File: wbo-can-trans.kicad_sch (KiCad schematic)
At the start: 7 parts, among them U15 TJA1051T-3

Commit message: Modified IGBTs and routed smart coils
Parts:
- renumbered C16 to C12, C17 to C13, C18 to C14, C19 to C15, D2 to D1, R16 to R15, U15 to U13
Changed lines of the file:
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@@
   (symbol (lib_id "Power_Protection:NUP2105L") (at 146.05 96.52 0) (mirror y)
     (in_bom yes) (on_board yes)
-    (property "Reference" "D2" (id 0) (at 140.97 95.25 0)
+    (property "Reference" "D1" (id 0) (at 140.97 95.25 0)
       (effects (font (size 1.27 1.27)) (justify left))
     )
@@
   (symbol (lib_id "Device:C") (at 105.41 77.47 0) (mirror y)
     (in_bom yes) (on_board yes)
-    (property "Reference" "C16" (id 0) (at 102.489 76.3016 0)
+    (property "Reference" "C12" (id 0) (at 102.489 76.3016 0)
       (effects (font (size 1.27 1.27)) (justify left))
     )
@@
   (symbol (lib_id "Device:C") (at 105.41 95.25 0) (mirror y)
     (in_bom yes) (on_board yes)
-    (property "Reference" "C17" (id 0) (at 102.489 94.0816 0)
+    (property "Reference" "C13" (id 0) (at 102.489 94.0816 0)
       (effects (font (size 1.27 1.27)) (justify left))
     )
@@
   (symbol (lib_id "Device:C") (at 190.5 93.98 0) (mirror y)
     (in_bom yes) (on_board yes)
-    (property "Reference" "C18" (id 0) (at 196.85 92.71 0)
+    (property "Reference" "C14" (id 0) (at 196.85 92.71 0)
       (effects (font (size 1.27 1.27)) (justify left))
     )
@@
   (symbol (lib_id "Device:C") (at 200.66 93.98 0) (mirror y)
     (in_bom yes) (on_board yes)
-    (property "Reference" "C19" (id 0) (at 207.01 92.71 0)
+    (property "Reference" "C15" (id 0) (at 207.01 92.71 0)
       (effects (font (size 1.27 1.27)) (justify left))
     )
@@
   (symbol (lib_id "Interface_CAN_LIN:TJA1051T-3") (at 166.37 86.36 0) (mirror y)
     (in_bom yes) (on_board yes)
-    (property "Reference" "U15" (id 0) (at 156.21 73.66 0))
+    (property "Reference" "U13" (id 0) (at 156.21 73.66 0))
     (property "Value" "TJA1051T-3" (id 1) (at 160.02 76.2 0))
     (property "Footprint" "Package_SO:SOIC-8_3.9x4.9mm_P1.27mm" (id 2) (at 166.37 99.06 0)
@@
   (symbol (lib_id "Device:R") (at 115.57 86.36 90) (mirror x)
     (in_bom no) (on_board yes)
-    (property "Reference" "R16" (id 0) (at 115.57 80.01 90))
+    (property "Reference" "R15" (id 0) (at 115.57 80.01 90))
     (property "Value" "120" (id 1) (at 115.57 82.55 90))
     (property "Footprint" "Resistor_SMD:R_1206_3216Metric" (id 2) (at 115.57 84.582 90)

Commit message: All fixed up for JLC
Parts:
- C16: renamed from C12; LCSC C1567 -> C14857
- C17: renamed from C13; LCSC C1567 -> C14857
- C18: renamed from C14; LCSC C1525 -> C49678
- C19: renamed from C15; LCSC C1525 -> C49678
- renumbered D1 to D2, R15 to R16, U13 to U15
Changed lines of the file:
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@@
   (symbol (lib_id "Power_Protection:NUP2105L") (at 146.05 96.52 0) (mirror y)
     (in_bom yes) (on_board yes)
-    (property "Reference" "D1" (id 0) (at 140.97 95.25 0)
+    (property "Reference" "D2" (id 0) (at 140.97 95.25 0)
       (effects (font (size 1.27 1.27)) (justify left))
     )
@@
   (symbol (lib_id "Device:C") (at 105.41 77.47 0) (mirror y)
     (in_bom yes) (on_board yes)
-    (property "Reference" "C12" (id 0) (at 102.489 76.3016 0)
+    (property "Reference" "C16" (id 0) (at 102.489 76.3016 0)
       (effects (font (size 1.27 1.27)) (justify left))
     )
@@
       (effects (font (size 1.27 1.27)) hide)
     )
-    (property "LCSC" "C1567" (id 4) (at 105.41 77.47 0)
+    (property "LCSC" "C14857" (id 4) (at 105.41 77.47 0)
       (effects (font (size 1.27 1.27)) hide)
     )
@@
   (symbol (lib_id "Device:C") (at 105.41 95.25 0) (mirror y)
     (in_bom yes) (on_board yes)
-    (property "Reference" "C13" (id 0) (at 102.489 94.0816 0)
+    (property "Reference" "C17" (id 0) (at 102.489 94.0816 0)
       (effects (font (size 1.27 1.27)) (justify left))
     )
@@
       (effects (font (size 1.27 1.27)) hide)
     )
-    (property "LCSC" "C1567" (id 4) (at 105.41 95.25 0)
+    (property "LCSC" "C14857" (id 4) (at 105.41 95.25 0)
       (effects (font (size 1.27 1.27)) hide)
     )
@@
   (symbol (lib_id "Device:C") (at 190.5 93.98 0) (mirror y)
     (in_bom yes) (on_board yes)
-    (property "Reference" "C14" (id 0) (at 196.85 92.71 0)
+    (property "Reference" "C18" (id 0) (at 196.85 92.71 0)
       (effects (font (size 1.27 1.27)) (justify left))
     )
@@
       (effects (font (size 1.27 1.27)) hide)
     )
-    (property "LCSC" "C1525" (id 4) (at 190.5 93.98 0)
+    (property "LCSC" "C49678" (id 4) (at 190.5 93.98 0)
       (effects (font (size 1.27 1.27)) hide)
     )
@@
   (symbol (lib_id "Device:C") (at 200.66 93.98 0) (mirror y)
     (in_bom yes) (on_board yes)
-    (property "Reference" "C15" (id 0) (at 207.01 92.71 0)
+    (property "Reference" "C19" (id 0) (at 207.01 92.71 0)
       (effects (font (size 1.27 1.27)) (justify left))
     )
@@
       (effects (font (size 1.27 1.27)) hide)
     )
-    (property "LCSC" "C1525" (id 4) (at 200.66 93.98 0)
+    (property "LCSC" "C49678" (id 4) (at 200.66 93.98 0)
       (effects (font (size 1.27 1.27)) hide)
     )
@@
   (symbol (lib_id "Interface_CAN_LIN:TJA1051T-3") (at 166.37 86.36 0) (mirror y)
     (in_bom yes) (on_board yes)
-    (property "Reference" "U13" (id 0) (at 156.21 73.66 0))
+    (property "Reference" "U15" (id 0) (at 156.21 73.66 0))
     (property "Value" "TJA1051T-3" (id 1) (at 160.02 76.2 0))
     (property "Footprint" "Package_SO:SOIC-8_3.9x4.9mm_P1.27mm" (id 2) (at 166.37 99.06 0)
@@
   (symbol (lib_id "Device:R") (at 115.57 86.36 90) (mirror x)
     (in_bom no) (on_board yes)
-    (property "Reference" "R15" (id 0) (at 115.57 80.01 90))
+    (property "Reference" "R16" (id 0) (at 115.57 80.01 90))
     (property "Value" "120" (id 1) (at 115.57 82.55 90))
     (property "Footprint" "Resistor_SMD:R_1206_3216Metric" (id 2) (at 115.57 84.582 90)

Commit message: Fixed 12V_RAW and added grounds for sensors
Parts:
- renumbered C16 to C12, C17 to C13, C18 to C14, C19 to C15, D2 to D1, R16 to R15, U15 to U13
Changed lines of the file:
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@@
   (symbol (lib_name "GND_22") (lib_id "power:GND") (at 105.41 99.06 0) (mirror y)
     (in_bom yes) (on_board yes)
-    (property "Reference" "#PWR0124" (id 0) (at 105.41 105.41 0)
+    (property "Reference" "#PWR0111" (id 0) (at 105.41 105.41 0)
       (effects (font (size 1.27 1.27)) hide)
     )
@@
   (symbol (lib_name "GND_24") (lib_id "power:GND") (at 166.37 96.52 0) (mirror y)
     (in_bom yes) (on_board yes)
-    (property "Reference" "#PWR0118" (id 0) (at 166.37 102.87 0)
+    (property "Reference" "#PWR0105" (id 0) (at 166.37 102.87 0)
       (effects (font (size 1.27 1.27)) hide)
     )
@@
   (symbol (lib_name "GND_27") (lib_id "power:GND") (at 181.61 91.44 90) (mirror x)
     (in_bom yes) (on_board yes)
-    (property "Reference" "#PWR0117" (id 0) (at 187.96 91.44 0)
+    (property "Reference" "#PWR0104" (id 0) (at 187.96 91.44 0)
       (effects (font (size 1.27 1.27)) hide)
     )
@@
   (symbol (lib_id "Power_Protection:NUP2105L") (at 146.05 96.52 0) (mirror y)
     (in_bom yes) (on_board yes)
-    (property "Reference" "D2" (id 0) (at 140.97 95.25 0)
+    (property "Reference" "D1" (id 0) (at 140.97 95.25 0)
       (effects (font (size 1.27 1.27)) (justify left))
     )
@@
   (symbol (lib_id "Device:C") (at 105.41 77.47 0) (mirror y)
     (in_bom yes) (on_board yes)
-    (property "Reference" "C16" (id 0) (at 102.489 76.3016 0)
+    (property "Reference" "C12" (id 0) (at 102.489 76.3016 0)
       (effects (font (size 1.27 1.27)) (justify left))
     )
@@
   (symbol (lib_name "GND_25") (lib_id "power:GND") (at 190.5 99.06 0) (mirror y)
     (in_bom yes) (on_board yes)
-    (property "Reference" "#PWR0123" (id 0) (at 190.5 105.41 0)
+    (property "Reference" "#PWR0110" (id 0) (at 190.5 105.41 0)
       (effects (font (size 1.27 1.27)) hide)
     )
@@
   (symbol (lib_name "GND_21") (lib_id "power:GND") (at 105.41 73.66 0) (mirror x)
     (in_bom yes) (on_board yes)
-    (property "Reference" "#PWR0125" (id 0) (at 105.41 67.31 0)
+    (property "Reference" "#PWR0112" (id 0) (at 105.41 67.31 0)
       (effects (font (size 1.27 1.27)) hide)
     )
@@
   (symbol (lib_name "GND_26") (lib_id "power:GND") (at 200.66 99.06 0) (mirror y)
     (in_bom yes) (on_board yes)
-    (property "Reference" "#PWR0122" (id 0) (at 200.66 105.41 0)
+    (property "Reference" "#PWR0109" (id 0) (at 200.66 105.41 0)
       (effects (font (size 1.27 1.27)) hide)
     )
@@
   (symbol (lib_id "Device:C") (at 105.41 95.25 0) (mirror y)
     (in_bom yes) (on_board yes)
-    (property "Reference" "C17" (id 0) (at 102.489 94.0816 0)
+    (property "Reference" "C13" (id 0) (at 102.489 94.0816 0)
       (effects (font (size 1.27 1.27)) (justify left))
     )
@@
   (symbol (lib_id "Device:C") (at 190.5 93.98 0) (mirror y)
     (in_bom yes) (on_board yes)
-    (property "Reference" "C18" (id 0) (at 196.85 92.71 0)
+    (property "Reference" "C14" (id 0) (at 196.85 92.71 0)
       (effects (font (size 1.27 1.27)) (justify left))
     )
@@
   (symbol (lib_id "Device:C") (at 200.66 93.98 0) (mirror y)
     (in_bom yes) (on_board yes)
-    (property "Reference" "C19" (id 0) (at 207.01 92.71 0)
+    (property "Reference" "C15" (id 0) (at 207.01 92.71 0)
       (effects (font (size 1.27 1.27)) (justify left))
     )
@@
   (symbol (lib_id "Interface_CAN_LIN:TJA1051T-3") (at 166.37 86.36 0) (mirror y)
     (in_bom yes) (on_board yes)
-    (property "Reference" "U15" (id 0) (at 156.21 73.66 0))
+    (property "Reference" "U13" (id 0) (at 156.21 73.66 0))
     (property "Value" "TJA1051T-3" (id 1) (at 160.02 76.2 0))
     (property "Footprint" "Package_SO:SOIC-8_3.9x4.9mm_P1.27mm" (id 2) (at 166.37 99.06 0)
@@
   (symbol (lib_name "GND_23") (lib_id "power:GND") (at 146.05 102.87 0) (mirror y)
     (in_bom yes) (on_board yes)
-    (property "Reference" "#PWR0121" (id 0) (at 146.05 109.22 0)
+    (property "Reference" "#PWR0108" (id 0) (at 146.05 109.22 0)
       (effects (font (size 1.27 1.27)) hide)
     )
@@
   (symbol (lib_id "Device:R") (at 115.57 86.36 90) (mirror x)
     (in_bom no) (on_board yes)
-    (property "Reference" "R16" (id 0) (at 115.57 80.01 90))
+    (property "Reference" "R15" (id 0) (at 115.57 80.01 90))
     (property "Value" "120" (id 1) (at 115.57 82.55 90))
     (property "Footprint" "Resistor_SMD:R_1206_3216Metric" (id 2) (at 115.57 84.582 90)

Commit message: convert to kicad7, add jumpers for direct drive igbt output
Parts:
- renumbered C12 to C16, C13 to C17, C14 to C18, C15 to C19, D1 to D2, R15 to R16, U13 to U15

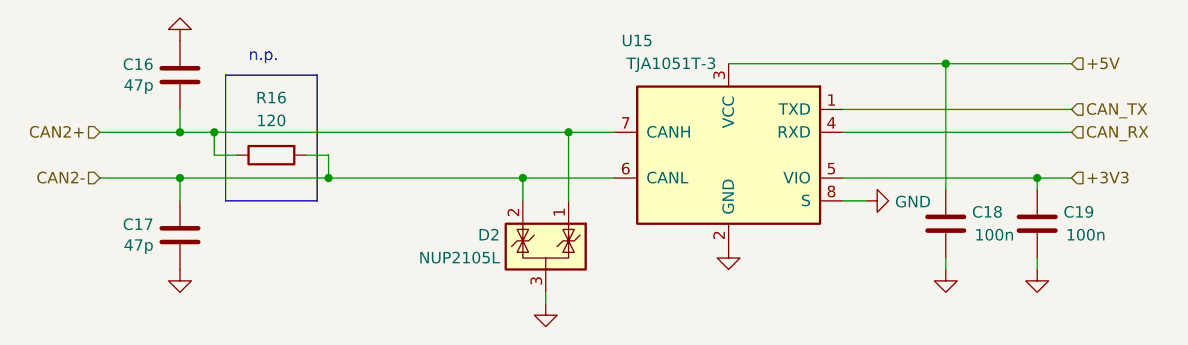
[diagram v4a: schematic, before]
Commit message: fix wideband library, ERC, DRC
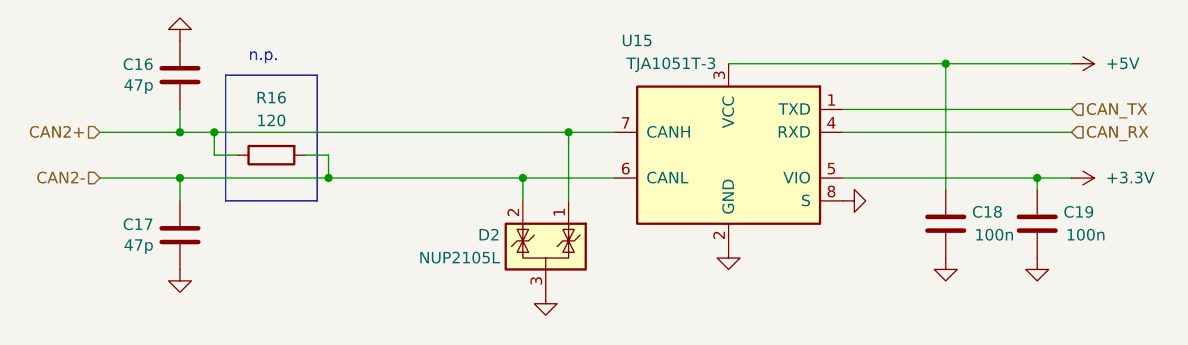
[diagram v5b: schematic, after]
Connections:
- net +3V3 renamed +3.3V

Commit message: schematic title blocks
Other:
- company: (none) -> FutureProofPerformance.com
- title: (none) -> Polygonus Universal 88p
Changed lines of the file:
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@@
 (kicad_sch (version 20230121) (generator eeschema)
   (paper "A4")
+  (title_block
+    (title "Polygonus Universal 88p")
+    (date "2023-11-12")
+    (rev "v1.0")
+    (company "FutureProofPerformance.com")
+  )
   (junction (at 148.59 83.82) (diameter 0) (color 0 0 0 0)
   )
